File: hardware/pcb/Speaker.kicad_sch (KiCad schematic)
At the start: 6 parts, among them U2 MAX98357AETE+T

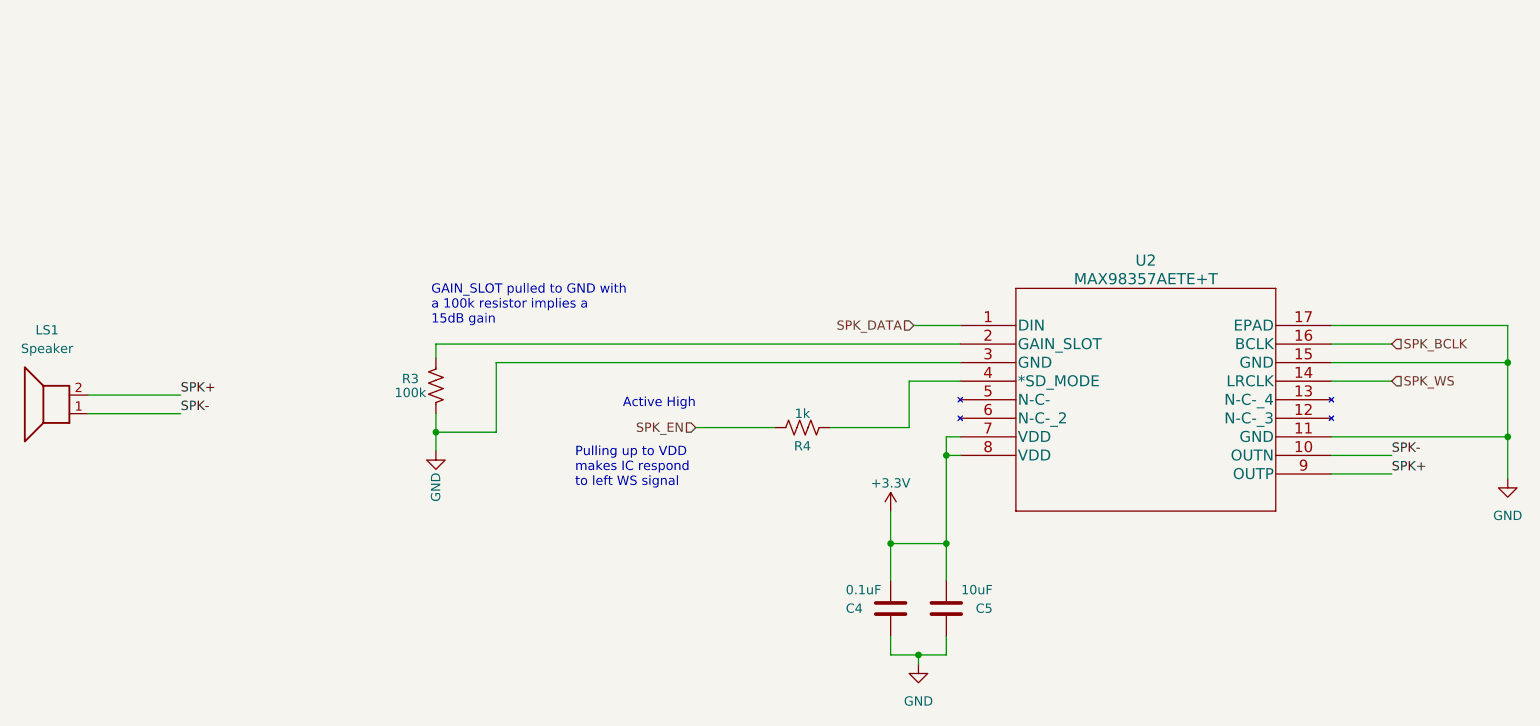
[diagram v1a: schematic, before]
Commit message: Replace third party MAX98357 symbol with custom one
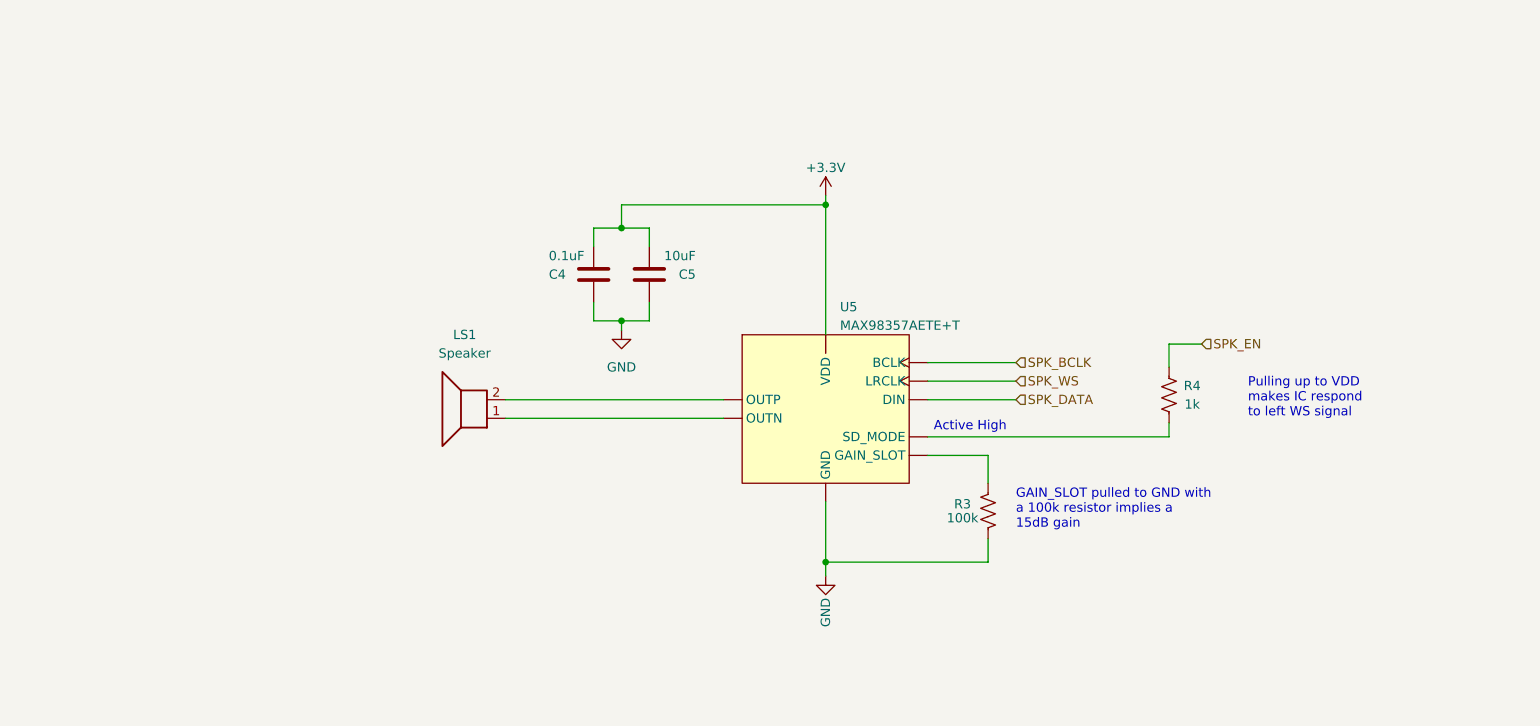
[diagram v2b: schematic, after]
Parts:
- removed U2: MAX98357AETE+T, MAX98357AETE+T:MAX98357AETE&plus_T, symbol MAX98357AETE+T:MAX98357AETE+T
- added U5: MAX98357AETE+T, Package_DFN_QFN:TQFN-16-1EP_3x3mm_P0.5mm_EP1.23x1.23mm, symbol MAX98357:MAX98357AETE+T
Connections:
- net +3.3V: now also U5.7 (VDD), U5.8 (VDD)
- net GND: now also U5.11 (GND), U5.15 (GND), U5.17 (Thermal), U5.3 (GND)
- net SPK_BCLK: now also U5.16 (BCLK)
- net SPK_DATA: now also U5.1 (DIN)
- net SPK_EN: now also R4.2; no longer R4.1
- net SPK_WS: now also U5.14 (LRCLK)
- net at R3.2: now also U5.2 (GAIN_SLOT)
- net SPK+: no longer names the net of LS1.2
- net SPK+: now also U5.9 (OUTP)
- net SPK-: no longer names the net of LS1.1
- net SPK-: now also U5.10 (OUTN)
- new net: R4.1, U5.4 (SD_MODE)
- new net: U5.12 (NC), U5.13 (NC), U5.5 (NC), U5.6 (NC)
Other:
- moved on the sheet: C4, C5, LS1, R3, R4

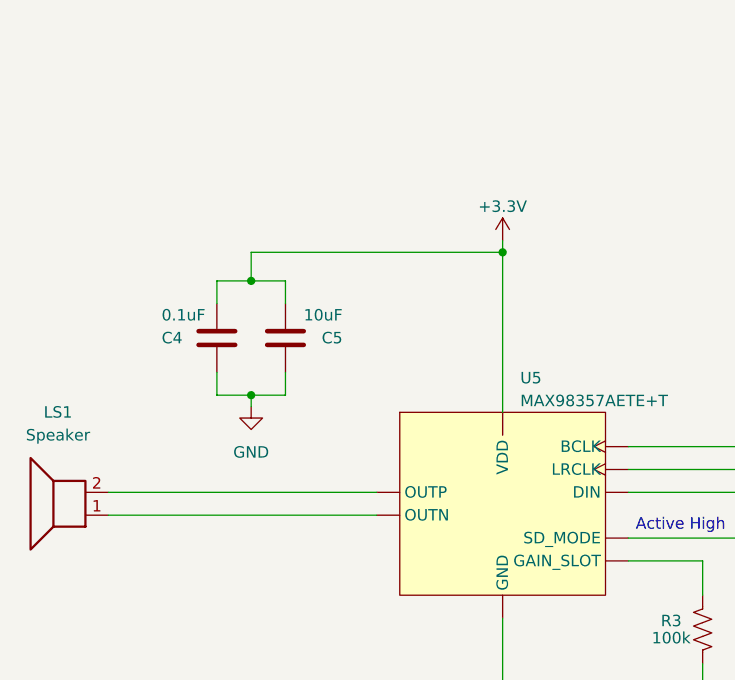
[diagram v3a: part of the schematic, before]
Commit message: Power speaker amplifier directly from battery
Also increase power trace widths
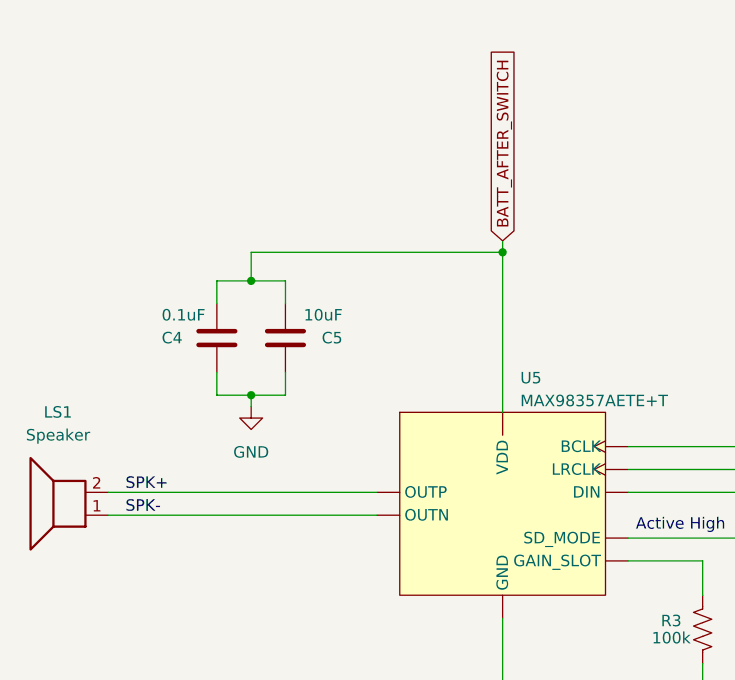
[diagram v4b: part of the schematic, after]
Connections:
- net SPK-: now reaches LS1.1, U5.10 (OUTN)
- net SPK+: now reaches LS1.2, U5.9 (OUTP)
- net +3.3V renamed VDD
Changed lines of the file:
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@@
     (effects (font (size 1.27 1.27)) (justify left bottom))
+  )
+  (label "SPK+" (at 109.855 99.06 0) (fields_autoplaced)
+    (effects (font (size 1.27 1.27)) (justify left bottom))
+  )
+  (label "SPK-" (at 109.855 101.6 0) (fields_autoplaced)
+    (effects (font (size 1.27 1.27)) (justify left bottom))
+  )
+  (global_label "BATT_AFTER_SWITCH" (shape input) (at 151.765 71.12 90) (fields_autoplaced)
+    (effects (font (size 1.27 1.27)) (justify left))
+    (property "Intersheetrefs" "${INTERSHEET_REFS}" (at 151.765 49.5876 90)
+      (effects (font (size 1.27 1.27)) (justify left) hide)
+    )
   )
   (hierarchical_label "SPK_BCLK" (shape input) (at 177.8 93.98 0) (fields_autoplaced)
@@
         )
       )
-    )
-  )
-  (symbol (lib_id "power:+3.3V") (at 151.765 71.12 0) (unit 1)
-    (in_bom yes) (on_board yes) (dnp no) (fields_autoplaced)
-    (property "Reference" "#PWR023" (at 151.765 74.93 0)
-      (effects (font (size 1.27 1.27)) hide)
-    )
-    (property "Value" "+3.3V" (at 151.765 67.31 0)
-      (effects (font (size 1.27 1.27)))
-    )
-    (property "Footprint" "" (at 151.765 71.12 0)
-      (effects (font (size 1.27 1.27)) hide)
-    )
-    (property "Datasheet" "" (at 151.765 71.12 0)
-      (effects (font (size 1.27 1.27)) hide)
-    )
-    (pin "1")
-    (instances
-      (project "Combadge"
-        (path "/dc42e7bc-f663-434d-8744-232038ac4fdf/8196ddf3-1455-4a17-8346-613907020849"
-          (reference "#PWR023") (unit 1)
-        )
-      )
